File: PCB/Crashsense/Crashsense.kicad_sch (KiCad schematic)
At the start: 0 parts

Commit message: pushing KICAD flies PCB schematic
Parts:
- added C1, C2, C4, C5: 10uF, symbol Device:C
- added C3: 1uF, symbol Device:C
- added C6: 100nF, symbol Device:C
- added D1: RLED, symbol Device:LED
- added D2: GLED, symbol Device:LED
- added J1: u-blox NEO-M8N, symbol Connector:Conn_01x04_Socket
- added J2: Micro_SD_Card_Det1, symbol Connector:Micro_SD_Card_Det1
- added J3: BATTERY_CONNECTOR, symbol Connector:Conn_01x02_Socket
- added P1: USB_C_Plug_USB2.0, symbol Connector:USB_C_Plug_USB2.0
- added R1: 5.1KR, symbol Device:R
- added R10, R11, R5, R6, R7, R8, R9: 10KR, symbol Device:R
- added R2: 1.2KR, symbol Device:R
- added R3, R4: 1kR, symbol Device:R
- added U1: ESP32-S3-WROOM-1, RF_Module:ESP32-S3-WROOM-1, symbol RF_Module:ESP32-S3-WROOM-1
- added U2: ADXL377, ADXL377:LFCSP-16-3X3, symbol ADXL377:ADXL377
- added U3: BMM150, Package_CSP:WLCSP-12_1.56x1.56mm_P0.4mm, symbol Sensor_Magnetic:BMM150
- added U4: DS3231M, Package_SO:SOIC-16W_7.5x10.3mm_P1.27mm, symbol Timer_RTC:DS3231M
- added U5: BMI270, BMI270:XDCR_BMI270, symbol BMI270:BMI270
- added U6: TP4056-42-ESOP8, Package_SO:SOIC-8-1EP_3.9x4.9mm_P1.27mm_EP2.41x3.3mm_ThermalVias, symbol Battery_Management:TP4056-42-ESOP8
- added U7: ME6211C10M5, Package_TO_SOT_SMD:SOT-23-5, symbol Regulator_Linear:ME6211C10M5
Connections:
- new net: R2.1, U6.2 (PROG)
- new net: D1.1 (K), U6.6 (~{STDBY})
- new net: D2.1 (K), U6.7 (~{CHRG})
- new net: P1.A5 (CC), R1.2
- new net: D2.2 (A), R4.2
- new net: U4.10 (GND), U4.11 (GND), U4.12 (GND), U4.13 (GND), U4.5 (GND), U4.6 (GND), U4.7 (GND), U4.8 (GND), U4.9 (GND)
- new net: U3.C5 (GND), U3.E1 (GND), U3.E3 (GND)
- new net: D1.2 (A), R3.2
- new net: U1.1 (GND), U1.40 (GND), U1.41 (GND)
- new net +5V_USB: C1.1, P1.A4 (VBUS), P1.A9 (VBUS), P1.B4 (VBUS), P1.B9 (VBUS), R3.1, R4.1, U6.4 (V_{CC}), U6.8 (CE)
- new net 3V3: C4.1, C5.1, C6.1, J1.1 (Pin_1), J2.4 (VDD), R10.2, R11.2, R5.2, R6.2, R7.2, R8.2, R9.2, U7.5 (V_{OUT})
- new net DAT1: J2.8 (DAT1), R10.1
- new net DAT2: J2.1 (DAT2), R9.1
- new net GND: C1.2, C2.2, C3.2, C4.2, C5.2, C6.2, J1.2 (Pin_2), J2.10 (SHIELD), J2.6 (VSS), J3.2 (Pin_2), P1.A1 (GND), P1.A12 (GND), P1.B1 (GND), P1.B12 (GND), P1.S1 (SHIELD), R1.1, R2.2, U6.1 (TEMP), U6.3 (GND), U6.9 (EPAD), U7.2 (V_{SS})
- new net GPS_RX: J1.4 (Pin_4)
- new net GPS_TX: J1.3 (Pin_3)
- new net SD_CS: J2.2 (DAT3/CD), R8.1
- new net SD_DET: J2.9 (DET), R11.1
- new net SD_MISO: J2.7 (DAT0), R5.1
- new net SD_MOSI: J2.3 (CMD), R7.1
- new net SD_SCK: J2.5 (CLK), R6.1
- new net USB_D+: P1.A6 (D+), U1.14 (USB_D+)
- new net USB_D-: P1.A7 (D-), U1.13 (USB_D-)
- new net VBAT: C2.1, C3.1, J3.1 (Pin_1), U6.5 (BAT), U7.1 (V_{IN}), U7.3 (CE)

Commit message: progressed on PCB and journalled for today
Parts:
- added BT1: Battery_Cell, symbol Device:Battery_Cell
- added C10, C8, C9: 10nF, symbol Device:C
- added C11, C12, C13, C7: 100nF, symbol Device:C
- added R12, R13: 4.7kR, symbol Device:R
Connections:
- net 3V3: now also U2.14 (VS@1), U2.15 (VS@2), U4.2 (VCC), U5.12 (CSB), U5.5 (VDDIO), U5.8 (VDD), C11.1, C12.1, C13.1, C7.1, R12.2, R13.2
- net GND: now also U2.2 (ST), U2.6 (GND@1), U2.7 (GND@2), U4.10 (GND), U4.11 (GND), U4.12 (GND), U4.13 (GND), U4.5 (GND), U4.6 (GND), U4.7 (GND), U4.8 (GND), U4.9 (GND), U5.1 (SDO), U5.6 (GNDIO), U5.7 (GND), BT1.2 (-), C10.2, C11.2, C12.2, C13.2, C7.2, C8.2, C9.2
- net GPS_RX: now also U1.10 (IO17)
- net GPS_TX: now also U1.11 (IO18)
- net SD_CS: now also U1.18 (IO10)
- net SD_DET: now also U1.17 (IO9)
- net SD_MISO: now also U1.21 (IO13)
- net SD_MOSI: now also U1.19 (IO11)
- net SD_SCK: now also U1.20 (IO12)
- net I2C_SCL: now reaches U5.13 (SCX)
- net I2C_SCL: now also U1.12 (IO8), U4.16 (SCL), R13.1
- net I2C_SDA: now reaches U5.14 (SDX)
- net I2C_SDA: now also U1.7 (IO7), U4.15 (SDA), R12.1
- net at U4.14 (VBAT): now also BT1.1 (+)
- net ACCEL_Z: now reaches U2.16 (ZOUT)
- net ACCEL_Z: now also U1.6 (IO6), C10.1
- net ACCEL_Y: now reaches U2.4 (YOUT)
- net ACCEL_Y: now also U1.5 (IO5), C9.1
- net ACCEL_X: now reaches U2.5 (XOUT)
- net ACCEL_X: now also U1.4 (IO4), C8.1
- no-connect marks 0 -> 5
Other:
- moved on the sheet: C1, C2, C3, C4, C5, C6, D1, D2, J1, J2, J3, P1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

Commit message: finished PCB and journalled
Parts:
- added C14, C16: 100nF, Capacitor_SMD:C_0805_2012Metric, symbol Device:C
- added C15: 10uF, Capacitor_SMD:C_0805_2012Metric, symbol Device:C
- added C17: 1uF, Capacitor_SMD:C_0805_2012Metric, symbol Device:C
- added J4: Debug_pins, Connector_PinHeader_2.54mm:PinHeader_1x02_P2.54mm_Vertical, symbol Connector:Conn_01x02_Socket
- added R14, R15: 10kR, Resistor_SMD:R_0805_2012Metric, symbol Device:R
- added SW1, SW2: SW_Push, Button_Switch_SMD:SW_SPST_SKQG_WithStem, symbol Switch:SW_Push
- BT1: footprint (none) -> Battery:BatteryHolder_Keystone_3034_1x20mm
- C1, C10, C11, C12, C13, C2, C3, C4, C5, C6, C7, C8, C9: footprint (none) -> Capacitor_SMD:C_0805_2012Metric
- D1, D2: footprint (none) -> LED_SMD:LED_0805_2012Metric
- J1: footprint (none) -> Connector_PinHeader_2.54mm:PinHeader_1x04_P2.54mm_Vertical
- J2: footprint (none) -> Connector_Card:microSD_HC_Hirose_DM3D-SF
- J3: footprint (none) -> Connector_JST:JST_PH_B2B-PH-K_1x02_P2.00mm_Vertical
- P1: footprint (none) -> Connector_USB:USB_C_Receptacle_HRO_TYPE-C-31-M-12
- R1, R10, R11, R12, R13, R2, R3, R4, R5, R6, R7, R8, R9: footprint (none) -> Resistor_SMD:R_0805_2012Metric
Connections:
- net 3V3: now also U1.2 (3V3), U3.A1 (PS), U3.A5 (CSB), U3.B2 (VDDIO), U3.E5 (VDD), C14.1, C15.2, C16.2, R14.2, R15.2
- net GND: now also U1.1 (GND), U1.40 (GND), U1.41 (GND), U3.C1 (SDO), U3.C5 (GND), U3.E1 (GND), U3.E3 (GND), C14.2, C15.1, C16.1, C17.2, SW1.1, SW2.1
- net I2C_SCL: now also U3.A3 (SCK)
- net I2C_SDA: now also U3.B4 (SDI)
- net IO0: now reaches U1.27 (IO0)
- net IO0: now also R15.1, SW2.2
- net EN: now reaches U1.3 (EN)
- net EN: now also C17.1, R14.1, SW1.2
- net RX: now reaches U1.36 (RXD0)
- net RX: now also J4.2 (Pin_2)
- net TX: now reaches U1.37 (TXD0)
- net TX: now also J4.1 (Pin_1)
- no-connect marks 5 -> 31
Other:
- moved on the sheet: BT1, C1, C10, C11, C12, C13, C2, C3, C4, C7, C8, C9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

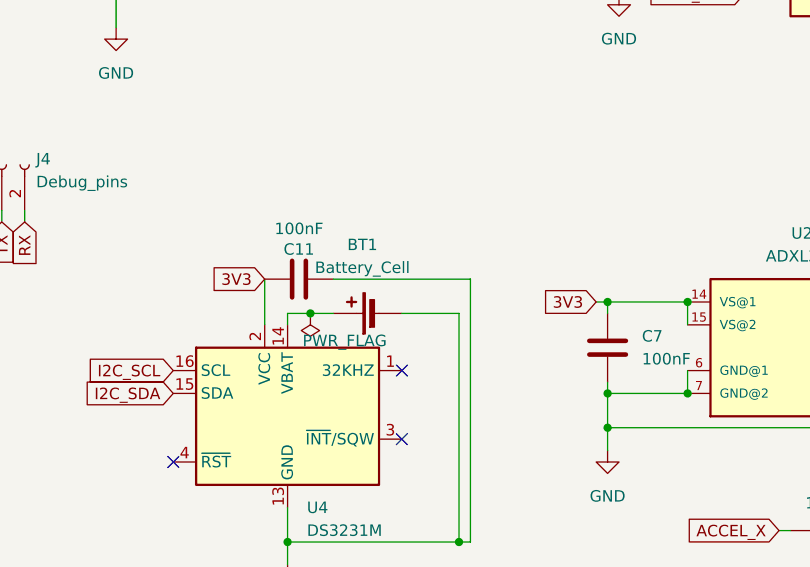
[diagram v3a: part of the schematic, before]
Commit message: Finished PCB componen placement and journalling
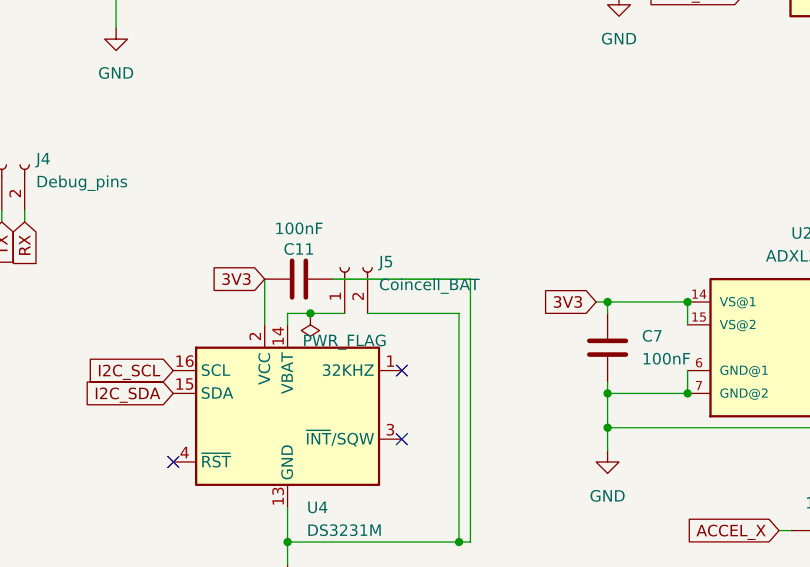
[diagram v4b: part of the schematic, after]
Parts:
- removed BT1: Battery_Cell, Battery:BatteryHolder_Keystone_3034_1x20mm, symbol Device:Battery_Cell
- added J5: Coincell_BAT, Connector_JST:JST_PH_B2B-PH-K_1x02_P2.00mm_Vertical, symbol Connector:Conn_01x02_Socket
- J2: footprint Connector_Card:microSD_HC_Hirose_DM3D-SF -> Connector_Card:microSD_HC_Hirose_DM3AT-SF-PEJM5
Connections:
- net GND: now also J5.2 (Pin_2)
- net at U4.14 (VBAT): now also J5.1 (Pin_1)
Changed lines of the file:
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@@
 	(wire
 		(pts
-			(xy 214.63 97.79) (xy 220.98 97.79)
-		)
-		(stroke
-			(width 0)
-			(type default)
-		)
-	)
-	(wire
-		(pts
 			(xy 208.28 144.78) (xy 212.09 144.78)
 		)
@@
 	(wire
 		(pts
+			(xy 210.82 97.79) (xy 220.98 97.79)
+		)
+		(stroke
+			(width 0)
+			(type default)
+		)
+	)
+	(wire
+		(pts
 			(xy 172.72 46.99) (xy 172.72 49.53)
 		)
@@
 	(wire
 		(pts
-			(xy 204.47 97.79) (xy 207.01 97.79)
+			(xy 204.47 97.79) (xy 208.28 97.79)
 		)
 		(stroke
@@
 	)
 	(symbol
+		(lib_id "Connector:Conn_01x02_Socket")
+		(at 208.28 92.71 90)
+		(unit 1)
+		(exclude_from_sim no)
+		(in_bom yes)
+		(on_board yes)
+		(dnp no)
+		(fields_autoplaced yes)
+		(property "Reference" "J5"
+			(at 212.09 92.0749 90)
+			(effects
+				(font
+					(size 1.27 1.27)
+				)
+				(justify right)
+			)
+		)
+		(property "Value" "Coincell_BAT"
+			(at 212.09 94.6149 90)
+			(effects
+				(font
+					(size 1.27 1.27)
+				)
+				(justify right)
+			)
+		)
+		(property "Footprint" "Connector_JST:JST_PH_B2B-PH-K_1x02_P2.00mm_Vertical"
+			(at 208.28 92.71 0)
+			(effects
+				(font
+					(size 1.27 1.27)
+				)
+				(hide yes)
+			)
+		)
+		(property "Datasheet" "~"
+			(at 208.28 92.71 0)
+			(effects
+				(font
+					(size 1.27 1.27)
+				)
+				(hide yes)
+			)
+		)
+		(property "Description" "Generic connector, single row, 01x02, script generated"
+			(at 208.28 92.71 0)
+			(effects
+				(font
+					(size 1.27 1.27)
+				)
+				(hide yes)
+			)
+		)
+		(pin "1"
+		)
+		(pin "2"
+		)
+		(instances
+			(project ""
+				(path "/ea8de0b3-15fb-4505-b68e-4a69daf0c69f"
+					(reference "J5")
+					(unit 1)
+				)
+			)
+		)
+	)
+	(symbol
 		(lib_id "Switch:SW_Push")
 		(at 78.74 113.03 90)
@@
 	)
 	(symbol
-		(lib_id "Device:Battery_Cell")
-		(at 212.09 97.79 90)
-		(unit 1)
-		(exclude_from_sim no)
-		(in_bom yes)
-		(on_board yes)
-		(dnp no)
-		(fields_autoplaced yes)
-		(property "Reference" "BT1"
-			(at 210.2485 90.17 90)
-			(effects
-				(font
-					(size 1.27 1.27)
-				)
-			)
-		)
-		(property "Value" "Battery_Cell"
-			(at 210.2485 92.71 90)
-			(effects
-				(font
-					(size 1.27 1.27)
-				)
-			)
-		)
-		(property "Footprint" "Battery:BatteryHolder_Keystone_3034_1x20mm"
-			(at 210.566 97.79 90)
-			(effects
-				(font
-					(size 1.27 1.27)
-				)
-				(hide yes)
-			)
-		)
-		(property "Datasheet" "~"
-			(at 210.566 97.79 90)
-			(effects
-				(font
-					(size 1.27 1.27)
-				)
-				(hide yes)
-			)
-		)
-		(property "Description" "Single-cell battery"
-			(at 212.09 97.79 0)
-			(effects
-				(font
-					(size 1.27 1.27)
-				)
-				(hide yes)
-			)
-		)
-		(property "Sim.Device" "V"
-			(at 212.09 97.79 0)
-			(effects
-				(font
-					(size 1.27 1.27)
-				)
-				(hide yes)
-			)
-		)
-		(property "Sim.Type" "DC"
-			(at 212.09 97.79 0)
-			(effects
-				(font
-					(size 1.27 1.27)
-				)
-				(hide yes)
-			)
-		)
-		(property "Sim.Pins" "1=+ 2=-"
-			(at 212.09 97.79 0)
-			(effects
-				(font
-					(size 1.27 1.27)
-				)
-				(hide yes)
-			)
-		)
-		(pin "2"
-		)
-		(pin "1"
-		)
-		(instances
-			(project ""
-				(path "/ea8de0b3-15fb-4505-b68e-4a69daf0c69f"
-					(reference "BT1")
-					(unit 1)
-				)
-			)
-		)
-	)
-	(symbol
 		(lib_id "power:GND")
 		(at 128.27 181.61 0)
@@
 			)
 		)
-		(property "Footprint" "Connector_Card:microSD_HC_Hirose_DM3D-SF"
+		(property "Footprint" "Connector_Card:microSD_HC_Hirose_DM3AT-SF-PEJM5"
 			(at -12.7 54.61 0)
 			(effects

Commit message: updated things
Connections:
- net GPS_RX: now also J1.3 (Pin_3); no longer J1.4 (Pin_4)
- net GPS_TX: now also J1.4 (Pin_4); no longer J1.3 (Pin_3)
